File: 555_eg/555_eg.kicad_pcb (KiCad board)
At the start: 2 copper layers, 29 x 106.5 mm, 45 parts, among them J1 Gate In, J2 Envelope Out, J3 Inverted Out, J4 Power Connector, Q1 2N3904, Q2 2N3904, Q3 2N3904, U1 NE555P, U2 TL074

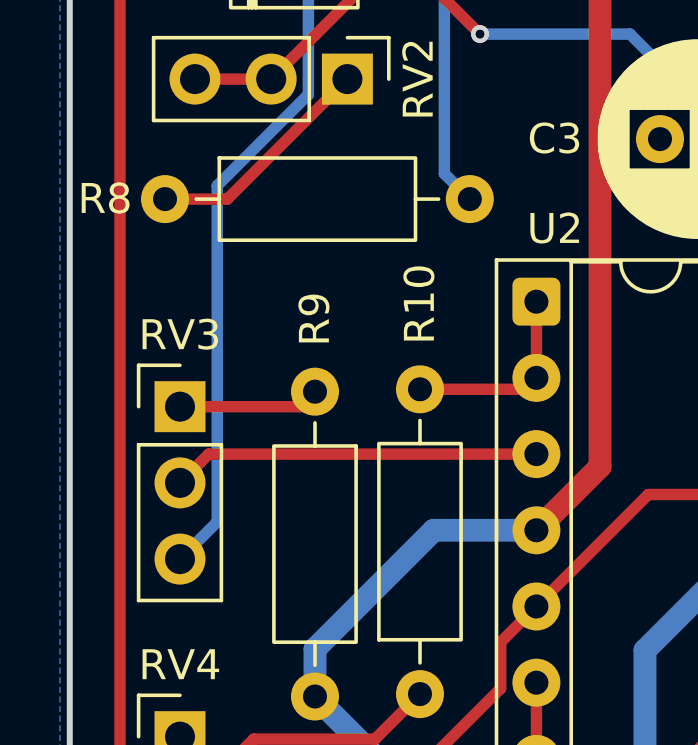
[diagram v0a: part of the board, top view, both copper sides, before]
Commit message: Swap out pot and resistor values for better ADSR values, fix sustain pot pins
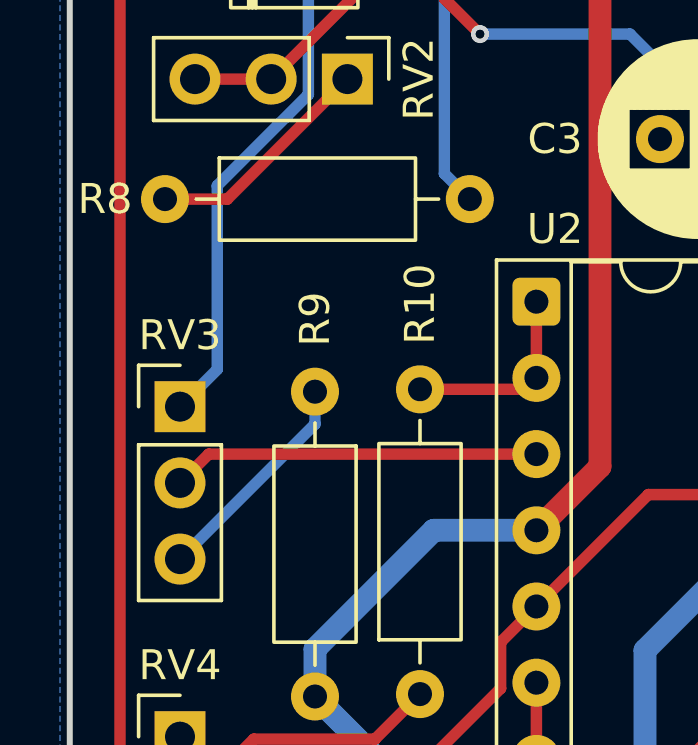
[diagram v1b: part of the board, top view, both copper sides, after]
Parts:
- R10, R7, R8: value 100k -> 220
- RV1, RV2, RV4: value A1M -> A100k
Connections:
- RV3 pad 1: Net-(R9-Pad1) -> Net-(U1-DIS)
- RV3 pad 3: Net-(U1-DIS) -> Net-(R9-Pad1)
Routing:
- net Net-(U1-DIS): track 25.5 -> 20.4 mm
- net Net-(R9-Pad1): track 4.71 -> 7.44 mm
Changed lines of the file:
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@@
 			)
 		)
-		(property "Value" "A1M"
+		(property "Value" "A100k"
 			(at 0 7.46 90)
 			(layer "F.Fab")
@@
 			(layers "*.Cu" "*.Mask")
 			(remove_unused_layers no)
-			(net 24 "Net-(R9-Pad1)")
+			(net 30 "Net-(U1-DIS)")
 			(pinfunction "1")
 			(pintype "passive")
@@
 			(layers "*.Cu" "*.Mask")
 			(remove_unused_layers no)
-			(net 30 "Net-(U1-DIS)")
+			(net 24 "Net-(R9-Pad1)")
 			(pinfunction "3")
 			(pintype "passive")
@@
 			)
 		)
-		(property "Value" "100k"
+		(property "Value" "220"
 			(at 5.08 2.37 0)
 			(layer "F.Fab")
@@
 			)
 		)
-		(property "Value" "A1M"
+		(property "Value" "A100k"
 			(at 0 7.46 0)
 			(layer "F.Fab")
@@
 			)
 		)
-		(property "Value" "100k"
+		(property "Value" "220"
 			(at 5.08 2.37 0)
 			(layer "F.Fab")
@@
 			)
 		)
-		(property "Value" "100k"
+		(property "Value" "220"
 			(at 5.08 2.37 90)
 			(layer "F.Fab")
@@
 			)
 		)
-		(property "Value" "A1M"
+		(property "Value" "A100k"
 			(at 0 7.46 0)
 			(layer "F.Fab")
@@
 	)
 	(segment
-		(start 139 93.42)
-		(end 143 93.42)
+		(start 143.5 94)
+		(end 143.5 92.92)
 		(width 0.381)
-		(layer "F.Cu")
+		(layer "B.Cu")
 		(net 24)
 	)
 	(segment
-		(start 143 93.42)
-		(end 143.5 92.92)
+		(start 139 98.5)
+		(end 143.5 94)
 		(width 0.381)
-		(layer "F.Cu")
+		(layer "B.Cu")
 		(net 24)
 	)
@@
 	)
 	(segment
-		(start 143.280001 83.015746)
-		(end 140.2415 86.054247)
+		(start 140.2415 86.054247)
+		(end 140.2415 92.1785)
 		(width 0.381)
 		(layer "B.Cu")
@@
 	)
 	(segment
-		(start 140.2415 97.2585)
-		(end 139 98.5)
+		(start 144.08 75.12)
+		(end 143.280001 75.919999)
 		(width 0.381)
 		(layer "B.Cu")
@@
 	)
 	(segment
-		(start 144.08 75.12)
-		(end 143.280001 75.919999)
+		(start 140.2415 92.1785)
+		(end 139 93.42)
 		(width 0.381)
 		(layer "B.Cu")
@@
 	)
 	(segment
-		(start 140.2415 86.054247)
-		(end 140.2415 97.2585)
+		(start 143.280001 83.015746)
+		(end 140.2415 86.054247)
 		(width 0.381)
 		(layer "B.Cu")
